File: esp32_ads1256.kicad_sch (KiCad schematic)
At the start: 24 parts, among them U1 ADS1256IDBR, Y1 Crystal

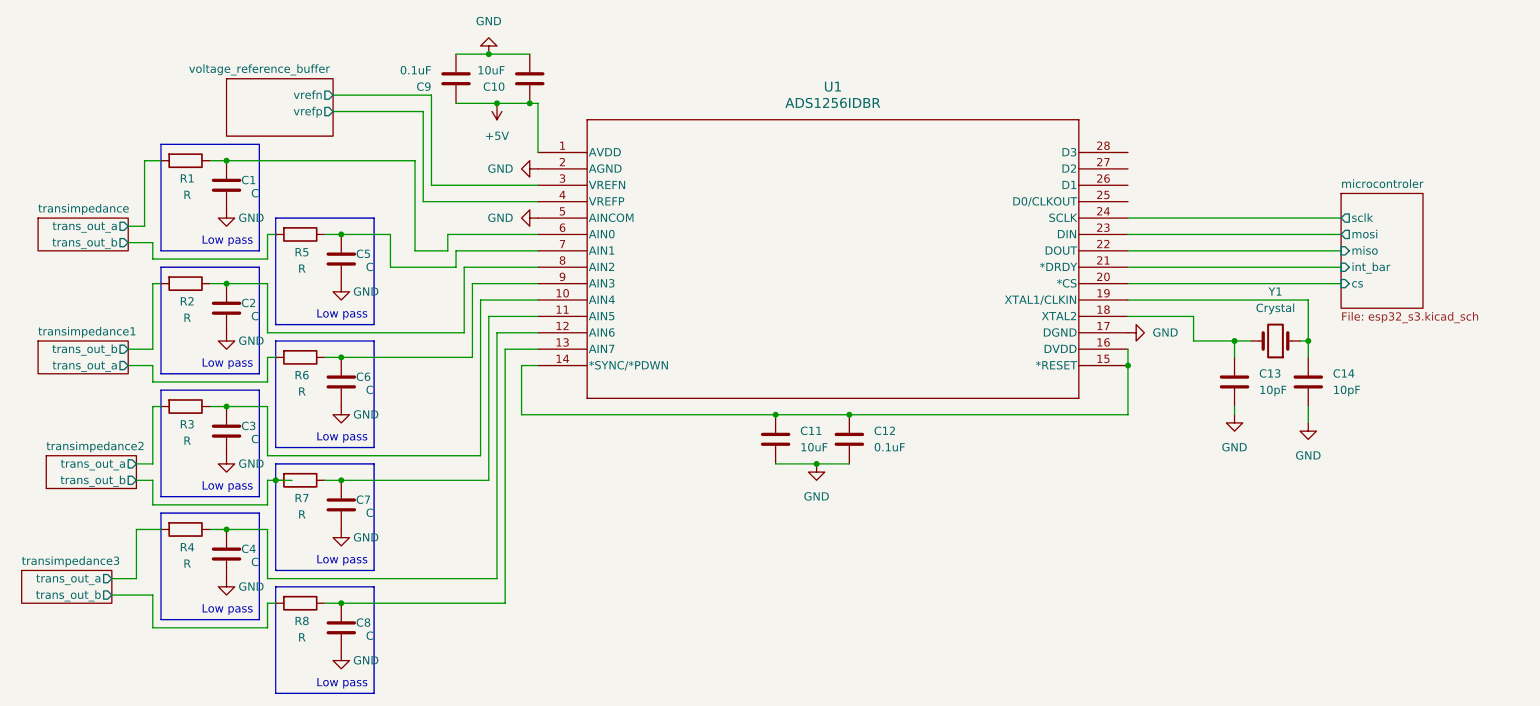
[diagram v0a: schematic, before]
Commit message: substituição do buffer de tensão com opa350 pela referencia de tensão ADR441xRZ
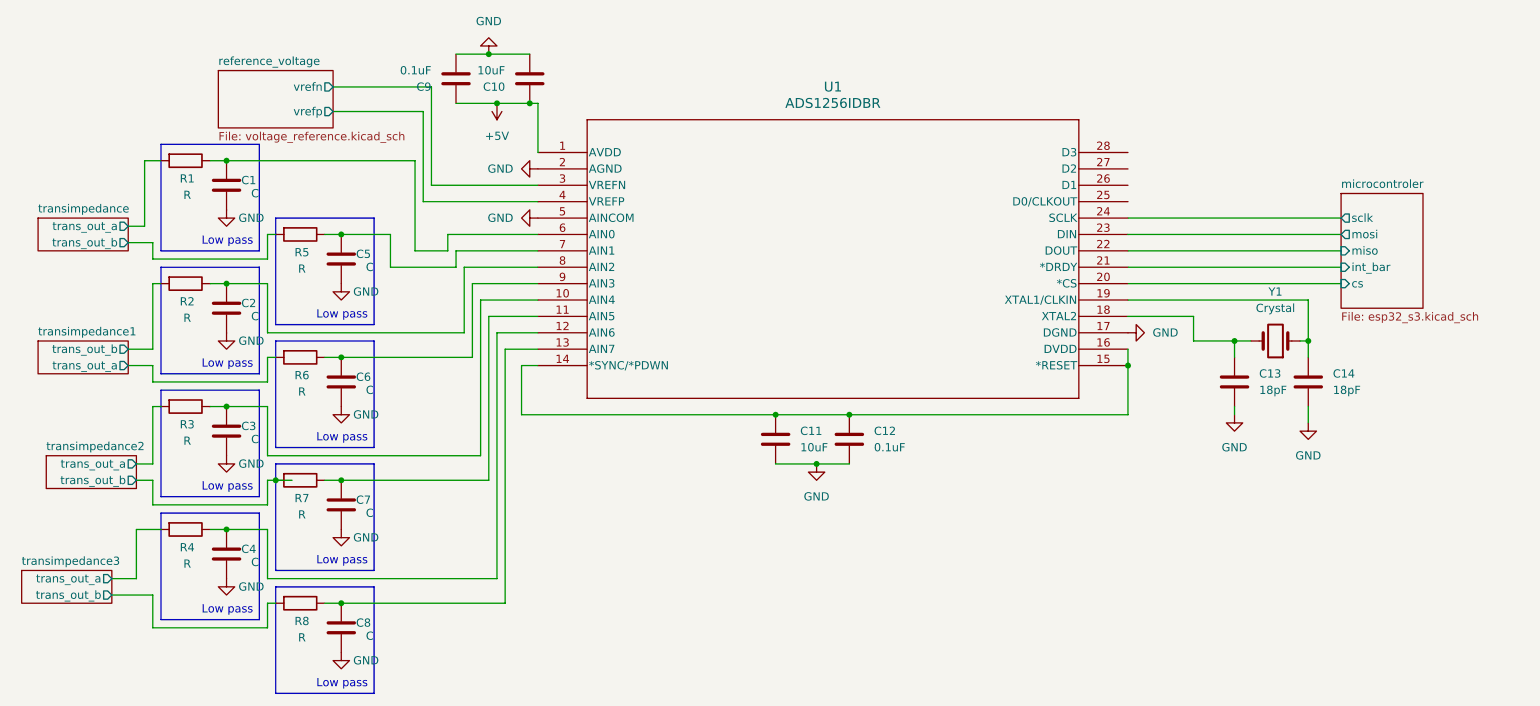
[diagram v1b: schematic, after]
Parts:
- C13, C14: value 10pF -> 18pF
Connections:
- net voltage_reference_buffer/vrefn renamed reference_voltage/vrefn
- net voltage_reference_buffer/vrefp renamed reference_voltage/vrefp
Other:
- removed sheet voltage_reference_buffer
- added sheet reference_voltage (voltage_reference.kicad_sch)
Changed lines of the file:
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@@
 	(wire
 		(pts
-			(xy 85.09 36.83) (xy 85.09 50.8)
+			(xy 85.09 35.56) (xy 85.09 50.8)
 		)
 		(stroke
@@
 	(wire
 		(pts
-			(xy 69.85 36.83) (xy 85.09 36.83)
+			(xy 69.85 35.56) (xy 85.09 35.56)
 		)
 		(stroke
@@
 			)
 		)
-		(property "Value" "10pF"
+		(property "Value" "18pF"
 			(at 224.79 82.5499 0)
 			(effects
@@
 			)
 		)
-		(property "Value" "10pF"
+		(property "Value" "18pF"
 			(at 213.36 82.5499 0)
 			(effects
@@
 		(on_board yes)
 		(dnp no)
-		(fields_autoplaced yes)
 		(property "Reference" "C9"
 			(at 85.09 35.5601 0)
@@
 	)
 	(sheet
+		(at 52.07 33.02)
+		(size 17.78 8.89)
+		(exclude_from_sim no)
+		(in_bom yes)
+		(on_board yes)
+		(dnp no)
+		(fields_autoplaced yes)
+		(stroke
+			(width 0.1524)
+			(type solid)
+		)
+		(fill
+			(color 0 0 0 0.0000)
+		)
+		(property "Sheetname" "reference_voltage"
+			(at 52.07 32.3084 0)
+			(effects
+				(font
+					(size 1.27 1.27)
+				)
+				(justify left bottom)
+			)
+		)
+		(property "Sheetfile" "voltage_reference.kicad_sch"
+			(at 52.07 42.4946 0)
+			(effects
+				(font
+					(size 1.27 1.27)
+				)
+				(justify left top)
+			)
+		)
+		(pin "vrefp" output
+			(at 69.85 39.37 0)
+			(effects
+				(font
+					(size 1.27 1.27)
+				)
+				(justify right)
+			)
+		)
+		(pin "vrefn" output
+			(at 69.85 35.56 0)
+			(effects
+				(font
+					(size 1.27 1.27)
+				)
+				(justify right)
+			)
+		)
+		(instances
+			(project "esp32_ads1256"
+				(path "/dbf90267-57f9-4f5a-8904-b91a6fafdaf7"
+					(page "8")
+				)
+			)
+		)
+	)
+	(sheet
 		(at 24.13 74.93)
 		(size 13.97 5.08)
@@
 				)
 			)
-		)
-	)
-	(sheet
-		(at 53.34 34.29)
-		(size 16.51 8.89)
-		(exclude_from_sim no)
-		(in_bom yes)
-		(on_board yes)
-		(dnp no)
-		(stroke
-			(width 0.1524)
-			(type solid)
-		)
-		(fill
-			(color 0 0 0 0.0000)
-		)
-		(property "Sheetname" "voltage_reference_buffer"
-			(at 47.498 33.528 0)
-			(effects
-				(font
-					(size 1.27 1.27)
-				)
-				(justify left bottom)
-			)
-		)
-		(property "Sheetfile" "vfb.kicad_sch"
-			(at 52.07 29.464 0)
-			(effects
-				(font
-					(size 1.27 1.27)
-				)
-				(justify left top)
-				(hide yes)
-			)
-		)
-		(pin "vrefp" output
-			(at 69.85 39.37 0)
-			(effects
-				(font
-					(size 1.27 1.27)
-				)
-				(justify right)
-			)
-		)
-		(pin "vrefn" output
-			(at 69.85 36.83 0)
-			(effects
-				(font
-					(size 1.27 1.27)
-				)
-				(justify right)
-			)
-		)
-		(instances
-			(project "esp32_ads1256"
-				(path "/dbf90267-57f9-4f5a-8904-b91a6fafdaf7"
-					(page "2")
-				)
-			)
